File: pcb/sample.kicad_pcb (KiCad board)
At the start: 2 copper layers, 50 x 50 mm, 14 parts, among them J1 Conn_Coaxial, J2 Conn_Coaxial

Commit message: apply output pos file
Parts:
- R1, R2, R3, R4, R5, R6: value ０ -> 0
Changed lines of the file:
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@@
 			)
 		)
-		(property "Value" "０"
+		(property "Value" "0"
 			(at 0 1.17 0)
 			(layer "F.Fab")
@@
 			)
 		)
-		(property "Value" "０"
+		(property "Value" "0"
 			(at 0 1.17 0)
 			(layer "F.Fab")
@@
 			)
 		)
-		(property "Value" "０"
+		(property "Value" "0"
 			(at 0 1.17 0)
 			(layer "F.Fab")
@@
 			)
 		)
-		(property "Value" "０"
+		(property "Value" "0"
 			(at 0 1.17 0)
 			(layer "F.Fab")
@@
 			)
 		)
-		(property "Value" "０"
+		(property "Value" "0"
 			(at 0 1.17 0)
 			(layer "F.Fab")
@@
 			)
 		)
-		(property "Value" "０"
+		(property "Value" "0"
 			(at 0 1.17 0)
 			(layer "F.Fab")

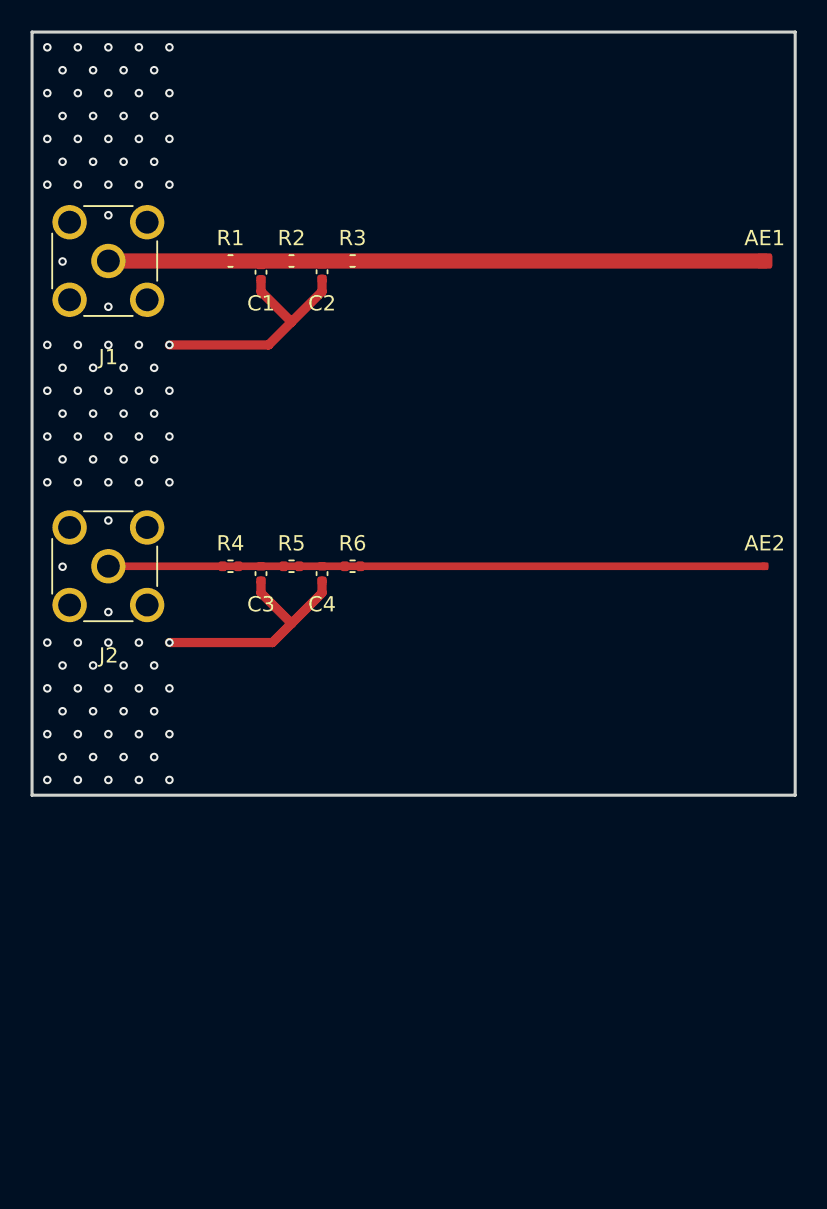
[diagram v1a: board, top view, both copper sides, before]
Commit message: modify KiCAD 9.0 to 8.0
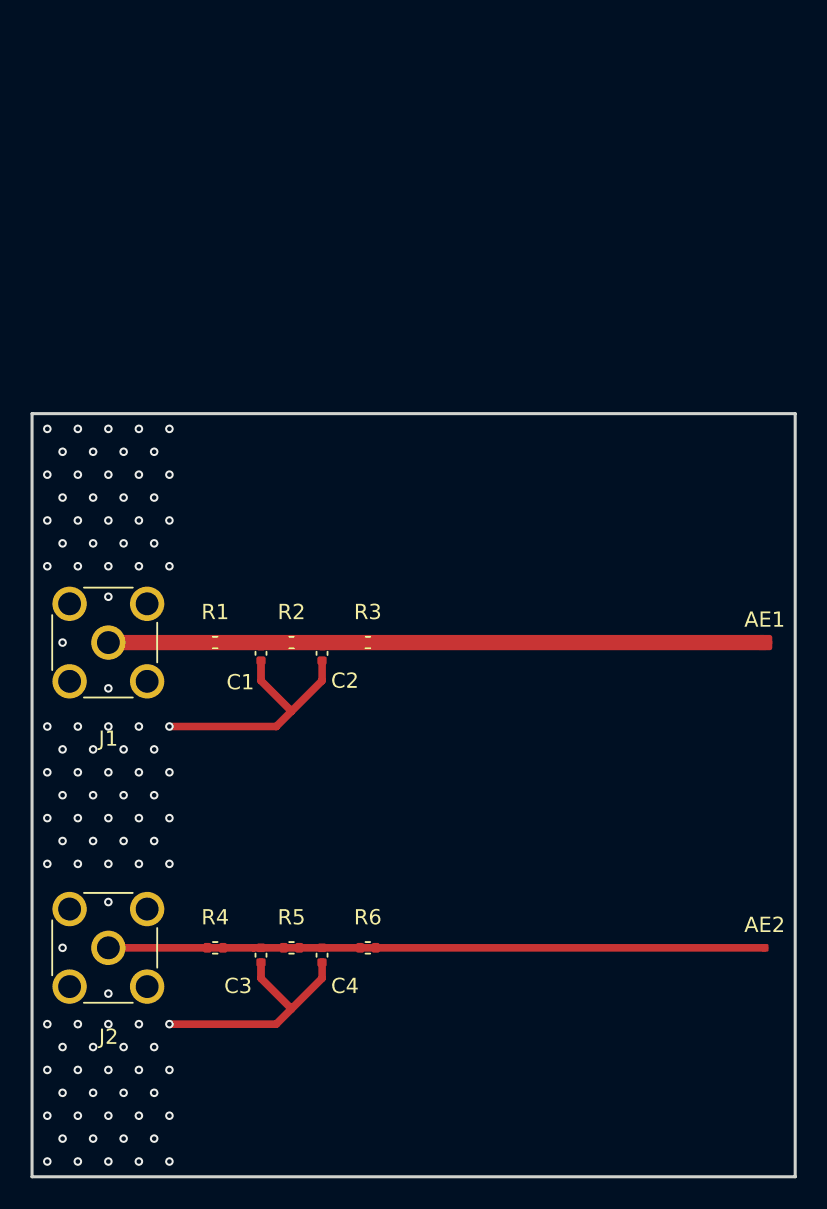
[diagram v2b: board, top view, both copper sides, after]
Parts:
- AE1: footprint RF_Antenna:Antenna_Stub_1.0mm -> sample:Antenna_Stub_1.0mm
- AE2: footprint RF_Antenna:Antenna_Stub_0.5mm -> sample:Antenna_Stub_0.5mm
- moved R1 25.0 mm to (112.0, 115.0)
- moved R3 25.0 mm to (122.0, 115.0)
- moved R4 25.0 mm to (112.0, 135.0)
- moved R6 25.0 mm to (122.0, 135.0)
- moved AE1 25.0 mm to (148.0, 115.0)
- moved AE2 25.0 mm to (148.0, 135.0)
- moved C2 25.0 mm to (119.0, 115.7)
- moved J1 25.0 mm to (105.0, 115.0)
- moved J2 25.0 mm to (105.0, 135.0)
- moved R2 25.0 mm to (117.0, 115.0)
- moved R5 25.0 mm to (117.0, 135.0)
- moved C3 25.0 mm to (115.0, 135.5)
- moved C4 25.0 mm to (119.0, 135.5)
- moved C1 25.0 mm to (115.0, 115.7)
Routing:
- net GND: track 31.6 -> 32.9 mm
